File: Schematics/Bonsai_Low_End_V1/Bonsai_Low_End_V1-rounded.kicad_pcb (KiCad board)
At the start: 4 copper layers, 31.9 x 20.2 mm, 26 parts, among them J1 Bat_Connector, U1 MOUDLE-SEEEDUINO-XIAO-ESP32C3, U2 MAX30101EFD, U3 1.8V, U5 DRV2605LDGS

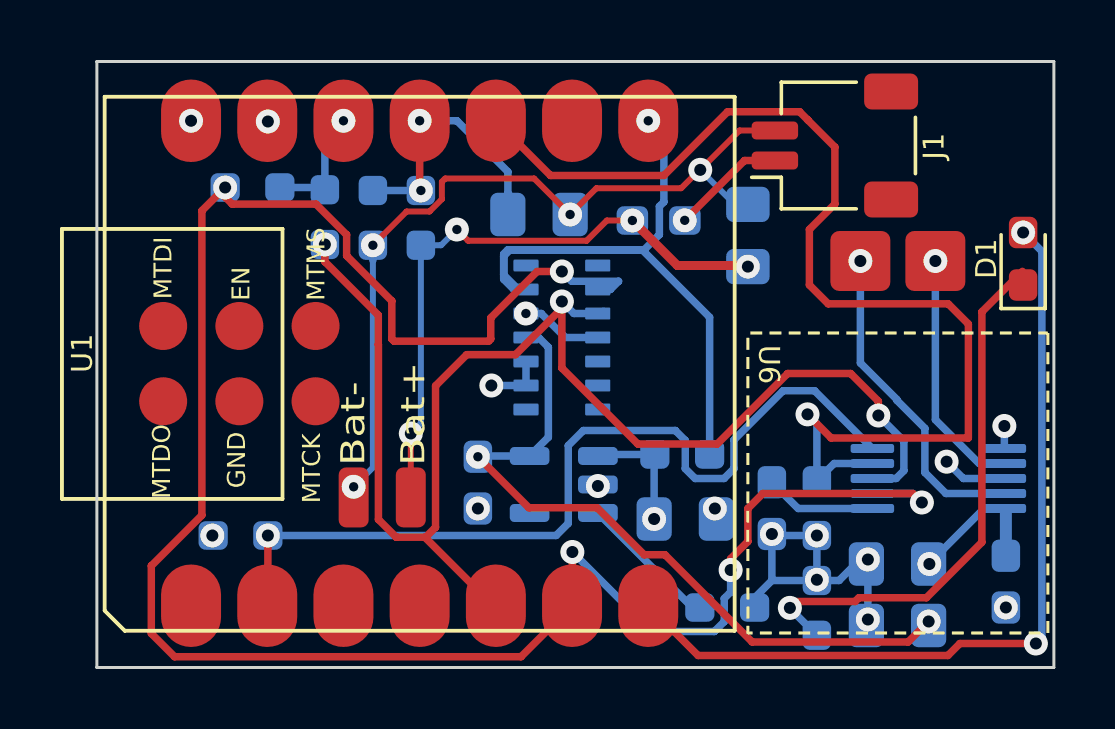
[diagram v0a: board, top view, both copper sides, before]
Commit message: rounded tracks
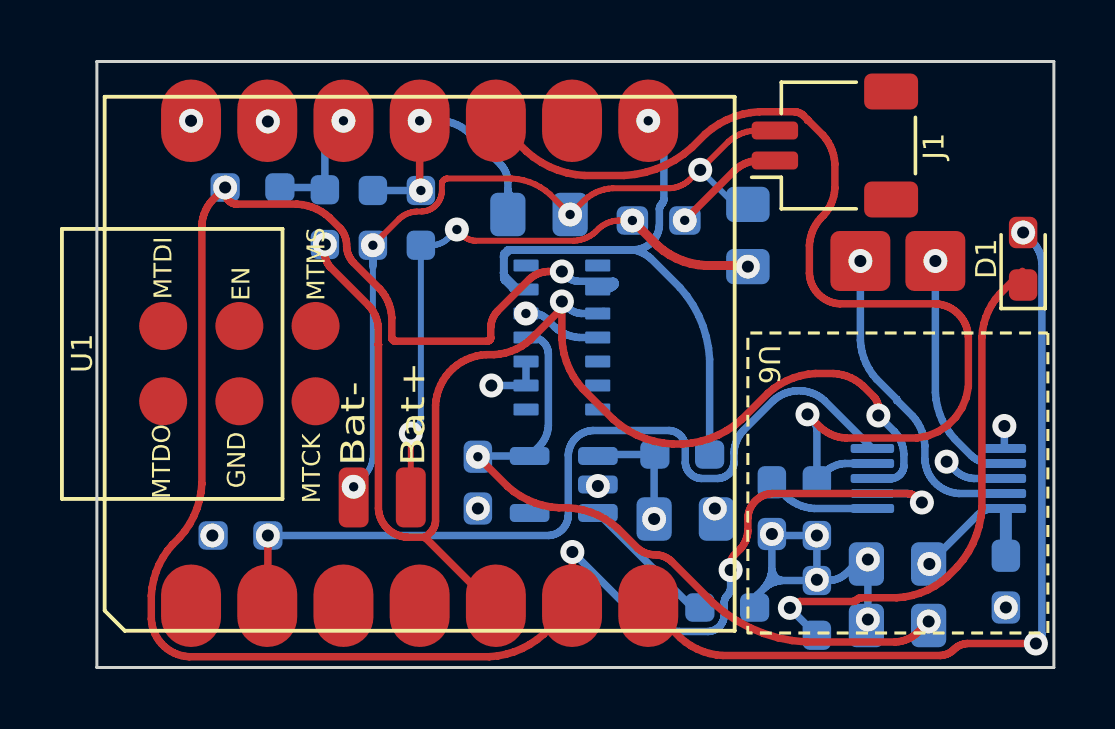
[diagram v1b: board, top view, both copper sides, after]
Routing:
- net DRV_IN/TRIG: track 38.1 -> 36.0 mm
- net SCL: track 69.9 -> 68.4 mm
- net GND: track 16.3 -> 17.7 mm
- net INT MAX: track 25.3 -> 26.7 mm
- net SDA: track 46.3 -> 45.2 mm
- net +1V8: track 24.7 -> 24.0 mm

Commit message: sent to jlcpcb
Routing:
- net DRV_IN/TRIG: track 36.0 -> 38.1 mm
- net GND: track 17.7 -> 16.3 mm
- net INT MAX: track 26.7 -> 25.3 mm
- net SDA: track 45.2 -> 46.4 mm
- net +1V8: track 24.0 -> 24.7 mm
- net SCL: track 68.4 -> 69.1 mm
- net FUN_LIGHT: track 28.8 -> 28.2 mm
